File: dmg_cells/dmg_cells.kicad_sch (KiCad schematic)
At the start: 956 parts, among them P1 PMOS, P10 PMOS, P11 PMOS, P12 PMOS, P13 PMOS, P14 PMOS, P15 PMOS, P16 PMOS, P17 PMOS, P18 PMOS, P19 PMOS, P2 PMOS, P20 PMOS, P21 PMOS, P22 PMOS, P23 PMOS, P24 PMOS, P3 PMOS, P4 PMOS, P5 PMOS, P6 PMOS, P7 PMOS, P8 PMOS, P9 PMOS

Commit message: Give more meaningful names to cell types
Before this commit, many of the cells types in the chip were named in a
sloppy manner. The different inverter, latch and flip flop valiants were
just suffixed with A, B, C, D, ... Those suffixes gave no information
about the actual differences. They had to be looked up in the
documentation. Now the names of cell types with different variants have
changed:

* Inverter types are named NOT_X1, NOT_X2, NOT_X3, ... The _Xn suffix
  reflects the drive strength of the cell. X1 is the drive strength of
  the weakest inverter, X2 is double the drive strength of the weakest
  inverter.
* Flip flop types are named DFFR, DFFR_CC, DFFR_CC_Q. DFFR is a normal
  data flip flop with reset and a single clock input. The suffix _CC is
  added to flip flops that have two complementary clock inputs (CLK and
  /CLK). Flip flops that only have the positive Q output are suffixed
  with _Q.
* Latch types are named similar to flip flops: DLATCH, DLATCH_EE,
  DLATCH_EE_Q. The suffix _EE is given to latches that require
  "externally inverted enable" signals (ENA and /ENA).
* I/O pad types all start with PAD_BIDIR, PAD_IN or PAD_OUT. They also
  have suffixes that describe what makes them unique, like _PU for
  pull-ups.

Other minor changes were made to align the names with common naming
schemes of other cell libraries.
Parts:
- U?: value D_LATCH_A -> DLATCH_EE; symbol DMG_CPU_Cells:D_LATCH_A -> DMG_CPU_Cells:DLATCH_EE
- U?: value NOR_8 -> NOR8; symbol DMG_CPU_Cells:NOR_8 -> DMG_CPU_Cells:NOR8
- U?: value OBUF_A -> PAD_OUT; symbol DMG_CPU_Cells:OBUF_A -> DMG_CPU_Cells:PAD_OUT
- U? (x30): value INVERTER_A -> NOT_X1; symbol DMG_CPU_Cells:INVERTER_A -> DMG_CPU_Cells:NOT_X1
- U?: value OBUF_B -> PAD_OUT_DIFF; symbol DMG_CPU_Cells:OBUF_B -> DMG_CPU_Cells:PAD_OUT_DIFF
- U?: value D_LATCH_A2 -> DLATCH_EE_Q; symbol DMG_CPU_Cells:D_LATCH_A2 -> DMG_CPU_Cells:DLATCH_EE_Q
- U?: value IOBUF_A -> PAD_BIDIR; symbol DMG_CPU_Cells:IOBUF_A -> DMG_CPU_Cells:PAD_BIDIR
- U?: value AO_2 -> AO22; symbol DMG_CPU_Cells:AO_2 -> DMG_CPU_Cells:AO22
- U? (x11): value AND_2 -> AND2; symbol DMG_CPU_Cells:AND_2 -> DMG_CPU_Cells:AND2
- U? (x8): value NOR_2 -> NOR2; symbol DMG_CPU_Cells:NOR_2 -> DMG_CPU_Cells:NOR2
- U?: value OA -> OA21; symbol DMG_CPU_Cells:OA -> DMG_CPU_Cells:OA21
- U?: value IOBUF_C -> PAD_BIDIR_SCK; symbol DMG_CPU_Cells:IOBUF_C -> DMG_CPU_Cells:PAD_BIDIR_SCK
- U?: value TRI_BUF_IF0 -> BUF_IF0; symbol DMG_CPU_Cells:TRI_BUF_IF0 -> DMG_CPU_Cells:BUF_IF0
- U?: value TFFD -> TFFNL; symbol DMG_CPU_Cells:TFFD -> DMG_CPU_Cells:TFFNL
- U?: value NOR_6 -> NOR6; symbol DMG_CPU_Cells:NOR_6 -> DMG_CPU_Cells:NOR6
- U? (x4): value NAND_2 -> NAND2; symbol DMG_CPU_Cells:NAND_2 -> DMG_CPU_Cells:NAND2
- U?: value AO_6 -> AO222222; symbol DMG_CPU_Cells:AO_6 -> DMG_CPU_Cells:AO222222
- U?: value DFFR_B -> DFFR_CC; symbol DMG_CPU_Cells:DFFR_B -> DMG_CPU_Cells:DFFR_CC
- U?: value AND_4 -> AND4; symbol DMG_CPU_Cells:AND_4 -> DMG_CPU_Cells:AND4
- U?: value INVERTER_D -> NOT_X4; symbol DMG_CPU_Cells:INVERTER_D -> DMG_CPU_Cells:NOT_X4
- U?: value OR_4 -> OR4; symbol DMG_CPU_Cells:OR_4 -> DMG_CPU_Cells:OR4
- U?: value INVERTER_C -> NOT_X3; symbol DMG_CPU_Cells:INVERTER_C -> DMG_CPU_Cells:NOT_X3
- U?: value INVERTER_B -> NOT_X2; symbol DMG_CPU_Cells:INVERTER_B -> DMG_CPU_Cells:NOT_X2
- U?: value NOR_3 -> NOR3; symbol DMG_CPU_Cells:NOR_3 -> DMG_CPU_Cells:NOR3
- U?: value INVERTER_E -> NOT_X6; symbol DMG_CPU_Cells:INVERTER_E -> DMG_CPU_Cells:NOT_X6
- U?: value NAND_7 -> NAND7; symbol DMG_CPU_Cells:NAND_7 -> DMG_CPU_Cells:NAND7
- U?: value OSC -> PAD_XTAL; symbol DMG_CPU_Cells:OSC -> DMG_CPU_Cells:PAD_XTAL
- U?: value NOR_5 -> NOR5; symbol DMG_CPU_Cells:NOR_5 -> DMG_CPU_Cells:NOR5
- U?: value IBUF_A -> PAD_IN; symbol DMG_CPU_Cells:IBUF_A -> DMG_CPU_Cells:PAD_IN
- U?: value IOBUF_B -> PAD_BIDIR_ENA_PU; symbol DMG_CPU_Cells:IOBUF_B -> DMG_CPU_Cells:PAD_BIDIR_ENA_PU
- U?: value D_LATCH_B -> DLATCH; symbol DMG_CPU_Cells:D_LATCH_B -> DMG_CPU_Cells:DLATCH
- U?: value DFFR_A -> DFFR_CC_Q; symbol DMG_CPU_Cells:DFFR_A -> DMG_CPU_Cells:DFFR_CC_Q
- U?: value AO_4 -> AO2222; symbol DMG_CPU_Cells:AO_4 -> DMG_CPU_Cells:AO2222
- U?: value NAND_3 -> NAND3; symbol DMG_CPU_Cells:NAND_3 -> DMG_CPU_Cells:NAND3
- U?: value DFFR_B2 -> DFFR; symbol DMG_CPU_Cells:DFFR_B2 -> DMG_CPU_Cells:DFFR
- U?: value OR_3 -> OR3; symbol DMG_CPU_Cells:OR_3 -> DMG_CPU_Cells:OR3
- U?: value IBUF_B -> PAD_IN_PU; symbol DMG_CPU_Cells:IBUF_B -> DMG_CPU_Cells:PAD_IN_PU
- U?: value NAND_4 -> NAND4; symbol DMG_CPU_Cells:NAND_4 -> DMG_CPU_Cells:NAND4
- U?: value TRI_INV_IF0 -> NOT_IF0; symbol DMG_CPU_Cells:TRI_INV_IF0 -> DMG_CPU_Cells:NOT_IF0
- U?: value NAND_6 -> NAND6; symbol DMG_CPU_Cells:NAND_6 -> DMG_CPU_Cells:NAND6
- U?: value TRI_INV_IF1 -> NOT_IF1; symbol DMG_CPU_Cells:TRI_INV_IF1 -> DMG_CPU_Cells:NOT_IF1
- U?: value NOR_4 -> NOR4; symbol DMG_CPU_Cells:NOR_4 -> DMG_CPU_Cells:NOR4
- U?: value OR_2 -> OR2; symbol DMG_CPU_Cells:OR_2 -> DMG_CPU_Cells:OR2
- U?: value AND_3 -> AND3; symbol DMG_CPU_Cells:AND_3 -> DMG_CPU_Cells:AND3
- U?: value AO_3 -> AO222; symbol DMG_CPU_Cells:AO_3 -> DMG_CPU_Cells:AO222
- U?: value OAI -> OAI21; symbol DMG_CPU_Cells:OAI -> DMG_CPU_Cells:OAI21
- U?: value AO_1 -> AO21; symbol DMG_CPU_Cells:AO_1 -> DMG_CPU_Cells:AO21
- U?: value NAND_5 -> NAND5; symbol DMG_CPU_Cells:NAND_5 -> DMG_CPU_Cells:NAND5
- U?: value DR_LATCH -> DRLATCH_EE; symbol DMG_CPU_Cells:DR_LATCH -> DMG_CPU_Cells:DRLATCH_EE
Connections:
- net COUT: now also U?.2 (SUM); no longer U?.1 (COUT)
- net Q: no longer N1.1 (D), N1.1 (D), N1.1 (D), N1.1 (D), N1.1 (D), N1.1 (D), N1.1 (D), N1.1 (D), N1.1 (D), N1.1 (D), N1.1 (D), N1.1 (D), N13.1 (D), N2.1 (D), N2.1 (D), N2.1 (D), N2.1 (D), N2.1 (D), N2.1 (D), N2.1 (D), N2.1 (D), N2.1 (D), N2.1 (D), N2.1 (D), N2.1 (D), N2.1 (D), N3.1 (D), N3.1 (D), N3.1 (D), N3.1 (D), N3.1 (D), N3.1 (D), N3.1 (D), N3.1 (D), N3.1 (D), N3.1 (D), N3.1 (D), N3.1 (D), N3.1 (D), N4.1 (D), N4.1 (D), N4.1 (D), N4.1 (D), N4.1 (D), N4.1 (D), N4.1 (D), N4.1 (D), N4.1 (D), N4.1 (D), N4.1 (D), N4.1 (D), N4.1 (D), N4.1 (D), N5.1 (D), N5.1 (D), N5.1 (D), N5.1 (D), N5.1 (D), N5.1 (D), N5.1 (D), N5.1 (D), N5.1 (D), N6.1 (D), N6.1 (D), N6.1 (D), N6.1 (D), N6.1 (D), N7.1 (D), N7.1 (D), N7.1 (D), N7.1 (D), N8.1 (D), N9.1 (D), N?.1 (D), P1.1 (D), P1.1 (D), P1.1 (D), P1.1 (D), P1.1 (D), P1.1 (D), P1.1 (D), P1.1 (D), P1.1 (D), P1.1 (D), P1.1 (D), P1.1 (D), P13.1 (D), P2.1 (D), P2.1 (D), P2.1 (D), P2.1 (D), P2.1 (D), P2.1 (D), P2.1 (D), P2.1 (D), P2.1 (D), P2.1 (D), P2.1 (D), P2.1 (D), P2.1 (D), P2.1 (D), P3.1 (D), P3.1 (D), P3.1 (D), P3.1 (D), P3.1 (D), P3.1 (D), P3.1 (D), P3.1 (D), P3.1 (D), P3.1 (D), P3.1 (D), P3.1 (D), P3.1 (D), P4.1 (D), P4.1 (D), P4.1 (D), P4.1 (D), P4.1 (D), P4.1 (D), P4.1 (D), P4.1 (D), P4.1 (D), P4.1 (D), P4.1 (D), P4.1 (D), P4.1 (D), P4.1 (D), P5.1 (D), P5.1 (D), P5.1 (D), P5.1 (D), P5.1 (D), P5.1 (D), P5.1 (D), P5.1 (D), P5.1 (D), P6.1 (D), P6.1 (D), P6.1 (D), P6.1 (D), P6.1 (D), P7.1 (D), P7.1 (D), P7.1 (D), P8.1 (D), P9.1 (D), P?.1 (D), U?.1, U?.1, U?.13, U?.2, U?.2, U?.2, U?.2, U?.2, U?.3, U?.3, U?.3, U?.3, U?.3, U?.3, U?.4, U?.4, U?.4, U?.4, U?.4, U?.4, U?.4, U?.4, U?.4, U?.4, U?.5, U?.5, U?.5, U?.5, U?.5, U?.6, U?.6, U?.7, U?.7, U?.7, U?.8, U?.9, U?.9
- net SUM: now also U?.1 (COUT); no longer U?.2 (SUM)
- net DRV_LOW renamed NDRV
- net ~{DRV}_HIGH renamed ~{PDRV}
- new net Y: N1.1 (D), N1.1 (D), N1.1 (D), N1.1 (D), N1.1 (D), N1.1 (D), N1.1 (D), N1.1 (D), N1.1 (D), N1.1 (D), N1.1 (D), N1.1 (D), N13.1 (D), N2.1 (D), N2.1 (D), N2.1 (D), N2.1 (D), N2.1 (D), N2.1 (D), N2.1 (D), N2.1 (D), N2.1 (D), N2.1 (D), N2.1 (D), N2.1 (D), N2.1 (D), N3.1 (D), N3.1 (D), N3.1 (D), N3.1 (D), N3.1 (D), N3.1 (D), N3.1 (D), N3.1 (D), N3.1 (D), N3.1 (D), N3.1 (D), N3.1 (D), N3.1 (D), N4.1 (D), N4.1 (D), N4.1 (D), N4.1 (D), N4.1 (D), N4.1 (D), N4.1 (D), N4.1 (D), N4.1 (D), N4.1 (D), N4.1 (D), N4.1 (D), N4.1 (D), N4.1 (D), N5.1 (D), N5.1 (D), N5.1 (D), N5.1 (D), N5.1 (D), N5.1 (D), N5.1 (D), N5.1 (D), N5.1 (D), N6.1 (D), N6.1 (D), N6.1 (D), N6.1 (D), N6.1 (D), N7.1 (D), N7.1 (D), N7.1 (D), N7.1 (D), N8.1 (D), N9.1 (D), N?.1 (D), P1.1 (D), P1.1 (D), P1.1 (D), P1.1 (D), P1.1 (D), P1.1 (D), P1.1 (D), P1.1 (D), P1.1 (D), P1.1 (D), P1.1 (D), P1.1 (D), P13.1 (D), P2.1 (D), P2.1 (D), P2.1 (D), P2.1 (D), P2.1 (D), P2.1 (D), P2.1 (D), P2.1 (D), P2.1 (D), P2.1 (D), P2.1 (D), P2.1 (D), P2.1 (D), P2.1 (D), P3.1 (D), P3.1 (D), P3.1 (D), P3.1 (D), P3.1 (D), P3.1 (D), P3.1 (D), P3.1 (D), P3.1 (D), P3.1 (D), P3.1 (D), P3.1 (D), P3.1 (D), P4.1 (D), P4.1 (D), P4.1 (D), P4.1 (D), P4.1 (D), P4.1 (D), P4.1 (D), P4.1 (D), P4.1 (D), P4.1 (D), P4.1 (D), P4.1 (D), P4.1 (D), P4.1 (D), P5.1 (D), P5.1 (D), P5.1 (D), P5.1 (D), P5.1 (D), P5.1 (D), P5.1 (D), P5.1 (D), P5.1 (D), P6.1 (D), P6.1 (D), P6.1 (D), P6.1 (D), P6.1 (D), P7.1 (D), P7.1 (D), P7.1 (D), P8.1 (D), P9.1 (D), P?.1 (D), U?.1, U?.1, U?.13, U?.2, U?.2, U?.2, U?.2, U?.2, U?.3, U?.3, U?.3, U?.3, U?.3, U?.3, U?.4, U?.4, U?.4, U?.4, U?.4, U?.4, U?.4, U?.4, U?.4, U?.4, U?.5, U?.5, U?.5, U?.5, U?.5, U?.6, U?.6, U?.7, U?.7, U?.7, U?.8, U?.9, U?.9
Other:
- note added: "AO21"
- note added: "AO22"
- note added: "AO222"
- note added: "AO2222"
- note added: "AO222222"
- note added: "BUF_IF0"
- note added: "DFFR"
- note added: "DFFR_CC"
- note added: "DFFR_CC_Q"
- note added: "DLATCH"
- note added: "DLATCH_EE"
- note added: "DLATCH_EE_Q"
- note added: "DRLATCH_EE"
- note added: "NOT gate with 1× drive strength"
- note added: "NOT gate with 2× drive strength"
- note added: "NOT gate with 3× drive strength"
- note added: "NOT gate with 4× drive strength"
- note added: "NOT gate with 6× drive strength"
- note added: "NOT_IF0"
- note added: "NOT_IF1"
- note added: "OA21"
- note added: "OAI21"
- note added: "PAD_BIDIR"
- note added: "PAD_BIDIR_ENA_PU"
- note added: "PAD_BIDIR_SCK"
- note added: "PAD_IN"
- note added: "PAD_IN_PU"
- note added: "PAD_OUT"
- note added: "PAD_OUT_DIFF"
- note added: "PAD_XTAL"
- note added: "ROM row select"
- note added: "TFFNL"
- note added: "TIE"
- note removed: "AO1"
- note removed: "AO2"
- note removed: "AO3"
- note removed: "AO4"
- note removed: "AO6"
- note removed: "CONST"
- note removed: "DFFR - Variant A"
- note removed: "DFFR - Variant B"
- note removed: "DFFR - Variant B2"
- note removed: "DR_LATCH"
- note removed: "D_LATCH - Variant A"
- note removed: "D_LATCH - Variant A2"
- note removed: "D_LATCH - Variant B"
- note removed: "IBUF_A"
- note removed: "IBUF_B"
- note removed: "INVERTER - Variant A"
- note removed: "INVERTER - Variant B"
- note removed: "INVERTER - Variant C"
- note removed: "INVERTER - Variant D"
- note removed: "INVERTER - Variant E"
- note removed: "IOBUF_A"
- note removed: "IOBUF_B"
- note removed: "IOBUF_C"
- note removed: "OA"
- note removed: "OAI"
- note removed: "OBUF_A"
- note removed: "OBUF_B"
- note removed: "OSC"
- note removed: "TFFD"
- note removed: "TRI_BUF_IF0"
- note removed: "TRI_INV_IF0"
- note removed: "TRI_INV_IF1"

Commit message: DMG Cells: Add FULL_ADD layout and schematic
Also update schematics for XOR, XNOR and HALF_ADD
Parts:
- removed N1 (x2), N2 (x2), N3 (x2), N4 (x3), N5 (x3), N6, N7, N8: NMOS, symbol DMG_CPU_Cells:NMOS
- removed P1 (x2), P2 (x2), P3 (x2), P4 (x3), P5 (x3), P6, P7, P8: PMOS, symbol DMG_CPU_Cells:PMOS
- added N1 (x3), N10, N11, N12, N13, N14, N15, N16, N2 (x3), N3 (x3), N4 (x4), N5 (x4), N6 (x2), N7 (x2), N8 (x2), N9: NMOS, symbol DMG_CPU_Cells:NMOS
- added P1 (x3), P10, P11, P12, P13, P14, P15, P16, P2 (x3), P3 (x3), P4 (x4), P5 (x4), P6 (x2), P7 (x2), P8 (x2), P9: PMOS, symbol DMG_CPU_Cells:PMOS
- added U? (x3): AND2, symbol DMG_CPU_Cells:AND2
- added U? (x3): NOR2, symbol DMG_CPU_Cells:NOR2
- added U? (x4): NAND2, symbol DMG_CPU_Cells:NAND2
- added U? (x3): XOR, symbol DMG_CPU_Cells:XOR
- added U? (x3): AO21, symbol DMG_CPU_Cells:AO21
- added U?: OR2, symbol DMG_CPU_Cells:OR2
- added U?: OAI21, symbol DMG_CPU_Cells:OAI21
- added U?: FULL_ADD, symbol DMG_CPU_Cells:FULL_ADD
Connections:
- net A: now also N10.2 (G), N12.2 (G), N16.2 (G), N4.2 (G), N8.2 (G), P10.2 (G), P12.2 (G), P16.2 (G), P4.2 (G), P8.2 (G), U?.1, U?.1, U?.2, U?.2, U?.2, U?.2 (1), U?.2 (1), U?.4 (A)
- net B: now also N11.2 (G), N13.2 (G), N15.2 (G), N5.2 (G), N7.2 (G), P11.2 (G), P13.2 (G), P15.2 (G), P5.2 (G), P7.2 (G), U?.1, U?.1, U?.1, U?.2, U?.2, U?.3 (2), U?.3 (2), U?.5 (B)
- net COUT: now also N9.1 (D), P8.1 (D), P9.1 (D), U?.3, U?.3, U?.3, U?.3 (COUT)
- net GND: now also N1.3 (S), N1.3 (S), N11.3 (S), N12.3 (S), N14.3 (S), N15.3 (S), N16.3 (S), N2.3 (S), N3.3 (S), N3.3 (S), N3.3 (S), N4.3 (S), N4.3 (S), N4.3 (S), N5.3 (S), N5.3 (S), N6.3 (S), N7.3 (S), N7.3 (S), N8.3 (S), N8.3 (S)
- net IN1: now also N1.2 (G), N1.2 (G), N5.2 (G), N5.2 (G), P1.2 (G), P1.2 (G), P5.2 (G), P5.2 (G), U?.1, U?.1, U?.2, U?.2
- net IN2: now also N2.2 (G), N2.2 (G), N4.2 (G), N4.2 (G), P2.2 (G), P2.2 (G), P4.2 (G), P4.2 (G), U?.1, U?.1, U?.2, U?.2
- net SUM: now also N3.1 (D), N4.1 (D), N5.1 (D), N6.1 (D), P4.1 (D), P4.1 (D), P5.1 (D), P5.1 (D), U?.1, U?.1, U?.2 (SUM), U?.4
- net VDD: now also P1.3 (S), P10.3 (S), P11.3 (S), P14.3 (S), P15.3 (S), P2.3 (S), P3.3 (S), P3.3 (S), P3.3 (S), P4.3 (S), P4.3 (S), P5.3 (S), P6.3 (S), P6.3 (S), P7.3 (S), P7.3 (S), P8.3 (S), P9.3 (S)
- net Y: now also N1.1 (D), N2.1 (D), N2.1 (D), N3.1 (D), P1.1 (D), P2.1 (D), P2.1 (D), P3.1 (D), U?.4, U?.4
- new net: N10.1 (D), N9.2 (G), P10.1 (D), P11.1 (D), P9.2 (G)
- new net: U?.3, U?.3 (x4)
- new net: N1.2 (G), N13.1 (D), N14.1 (D), N5.2 (G), N6.2 (G), P1.2 (G), P12.1 (D), P13.1 (D), P5.2 (G), P6.2 (G)
- new net: P12.3 (S), P13.3 (S), P14.1 (D)
- new net: N3.2 (G), N4.1 (D), N5.1 (D), P3.2 (G), P5.1 (D)
- new net: N6.2 (G), N7.1 (D), N8.1 (D), P6.2 (G), P8.1 (D)
- new net: N4.1 (D), N5.3 (S) (x2)
- new net: N10.3 (S), N11.1 (D)
- new net: N14.2 (G), N15.1 (D), N16.1 (D), P14.2 (G), P16.1 (D)
- new net: P15.1 (D), P16.3 (S)
- new net: N3.2 (G), N5.1 (D), P3.2 (G), P4.1 (D), P5.1 (D)
- new net: P1.3 (S), P2.3 (S), P3.1 (D)
- new net: U?.1, U?.2, U?.2 (1)
- new net: P1.1 (D), P2.3 (S)
- new net: P3.1 (D), P4.3 (S), P5.3 (S)
- new net: N1.1 (D), N2.1 (D), N3.2 (G), P1.1 (D), P3.2 (G)
- new net: U?.1, U?.3 (x2)
- new net: U?.1, U?.2, U?.2, U?.4
- new net: N6.1 (D), N8.2 (G), P6.1 (D), P7.1 (D), P8.2 (G)
- new net: N6.3 (S), N7.1 (D)
- new net: P4.3 (S), P5.3 (S), P6.1 (D)
- new net: P7.1 (D), P8.3 (S)
- new net: U?.2, U?.3 (x2)
- new net: N1.1 (D), N2.3 (S)
- new net: N8.1 (D), N9.3 (S)
- new net: N12.1 (D), N13.3 (S)
- new net: N1.3 (S), N2.3 (S), N3.1 (D)
- new net: P1.3 (S), P2.1 (D)
- new net: N4.3 (S), N5.1 (D)
- new net: P4.1 (D), P5.3 (S)
- new net CIN: N2.2 (G), N4.2 (G), N7.2 (G), P2.2 (G), P4.2 (G), P7.2 (G), U?.1, U?.1, U?.1, U?.1 (CIN), U?.2, U?.3 (2)
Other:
- note added: "FULL_ADD"
- moved on the sheet: N1, N2, N3, P1, P2, P3

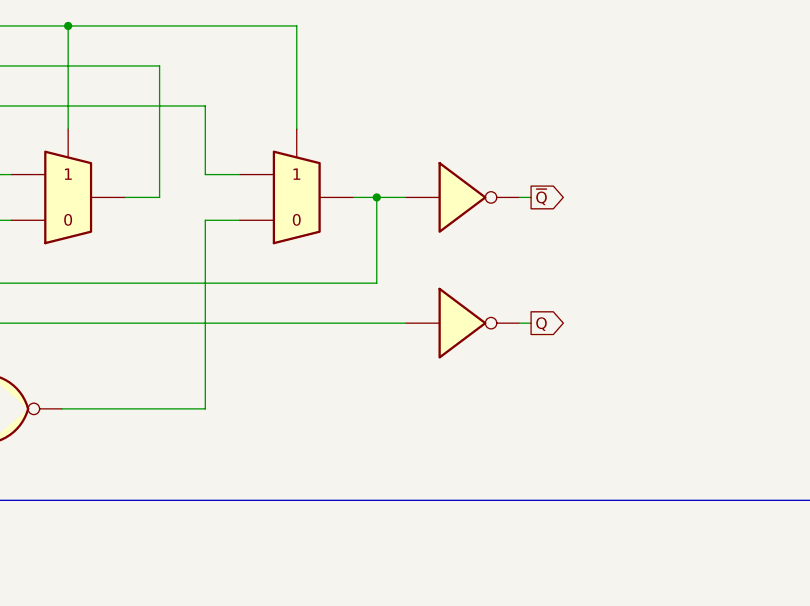
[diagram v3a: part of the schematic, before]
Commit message: DMG Cells: Fix DFFSR schematic
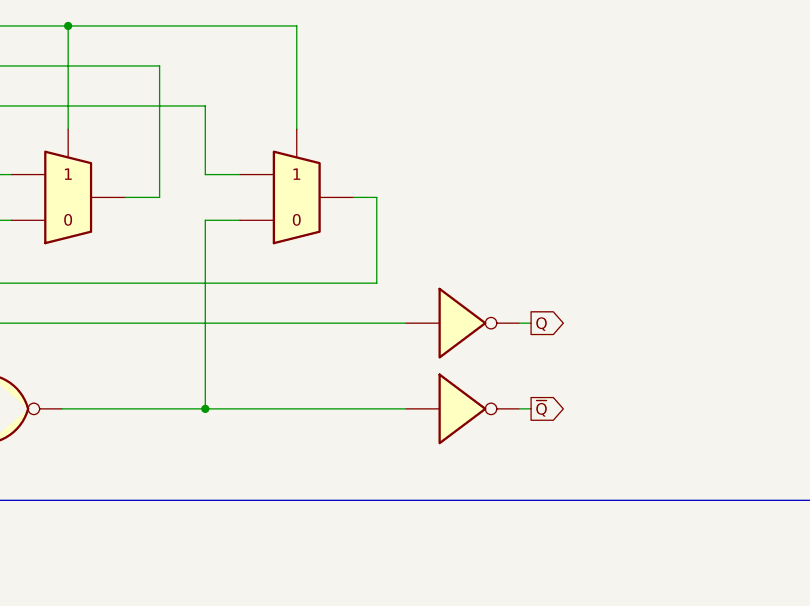
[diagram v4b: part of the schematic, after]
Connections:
- net at U?.3, U?.3: now also U?.1
- net at U?.1, U?.4: no longer U?.1
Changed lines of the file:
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@@
 	(title_block
 		(title "DMG CPU B Cells")
-		(date "2026-02-17")
+		(date "2026-02-19")
 		(rev "0")
 		(company "CC-BY-SA-4.0 Régis Galland & Michael Singer")
@@
 	)
 	(junction
+		(at 149.225 956.945)
+		(diameter 0)
+		(color 0 0 0 0)
+	)
+	(junction
 		(at 858.52 364.49)
 		(diameter 0)
@@
 	)
 	(junction
-		(at 168.275 933.45)
-		(diameter 0)
-		(color 0 0 0 0)
-	)
-	(junction
 		(at 580.39 593.09)
 		(diameter 0)
@@
 	(wire
 		(pts
+			(xy 149.225 956.945) (xy 171.45 956.945)
+		)
+		(stroke
+			(width 0)
+			(type default)
+		)
+	)
+	(wire
+		(pts
 			(xy 988.06 561.34) (xy 988.06 567.69)
 		)
@@
 	(wire
 		(pts
-			(xy 168.275 933.45) (xy 171.45 933.45)
-		)
-		(stroke
-			(width 0)
-			(type default)
-		)
-	)
-	(wire
-		(pts
 			(xy 57.15 176.53) (xy 76.2 176.53)
 		)
@@
 	(wire
 		(pts
-			(xy 184.15 933.45) (xy 185.42 933.45)
+			(xy 184.15 956.945) (xy 185.42 956.945)
 		)
 		(stroke
@@
 	(global_label "~{Q}"
 		(shape output)
-		(at 185.42 933.45 0)
+		(at 185.42 956.945 0)
 		(fields_autoplaced yes)
 		(effects
@@
 		)
 		(property "Intersheetrefs" "${INTERSHEET_REFS}"
-			(at 189.6563 933.45 0)
+			(at 189.6563 956.945 0)
 			(effects
 				(font
@@
 	(symbol
 		(lib_id "DMG_CPU_Cells:NOT_X1")
-		(at 177.8 933.45 0)
+		(at 177.8 956.945 0)
 		(unit 1)
 		(exclude_from_sim no)
@@
 		(dnp no)
 		(property "Reference" "U?"
-			(at 177.8 928.37 0)
+			(at 177.8 951.865 0)
 			(effects
 				(font
@@
 		)
 		(property "Value" "NOT_X1"
-			(at 177.8 938.53 0)
+			(at 177.8 962.025 0)
 			(effects
 				(font
@@
 		)
 		(property "Footprint" ""
-			(at 175.26 933.45 0)
+			(at 175.26 956.945 0)
 			(effects
 				(font
@@
 		)
 		(property "Datasheet" "http://iceboy.a-singer.de/doc/dmg_cells.html#not_x1"
-			(at 179.07 941.07 0)
+			(at 179.07 964.565 0)
 			(effects
 				(font
@@
 		)
 		(property "Description" "Simple inverter."
-			(at 177.8 933.45 0)
+			(at 177.8 956.945 0)
 			(effects
 				(font
